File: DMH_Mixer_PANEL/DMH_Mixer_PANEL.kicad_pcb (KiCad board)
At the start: 2 copper layers, 50 x 200 mm, 5 parts, among them J0 Panel_GND_Solder_Wire_Pad

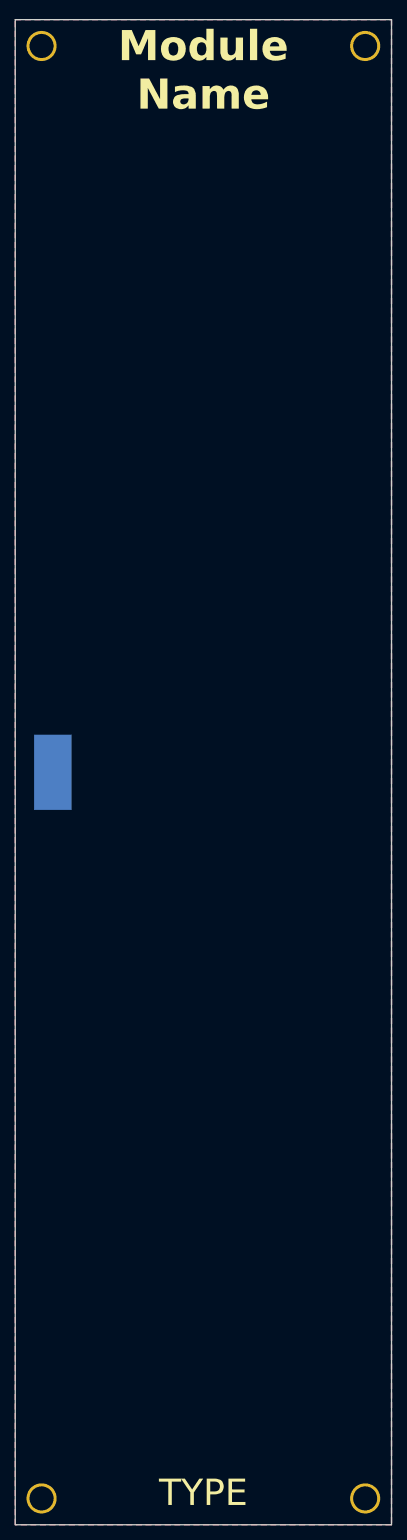
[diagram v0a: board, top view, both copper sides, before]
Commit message: Designed mixer front panel
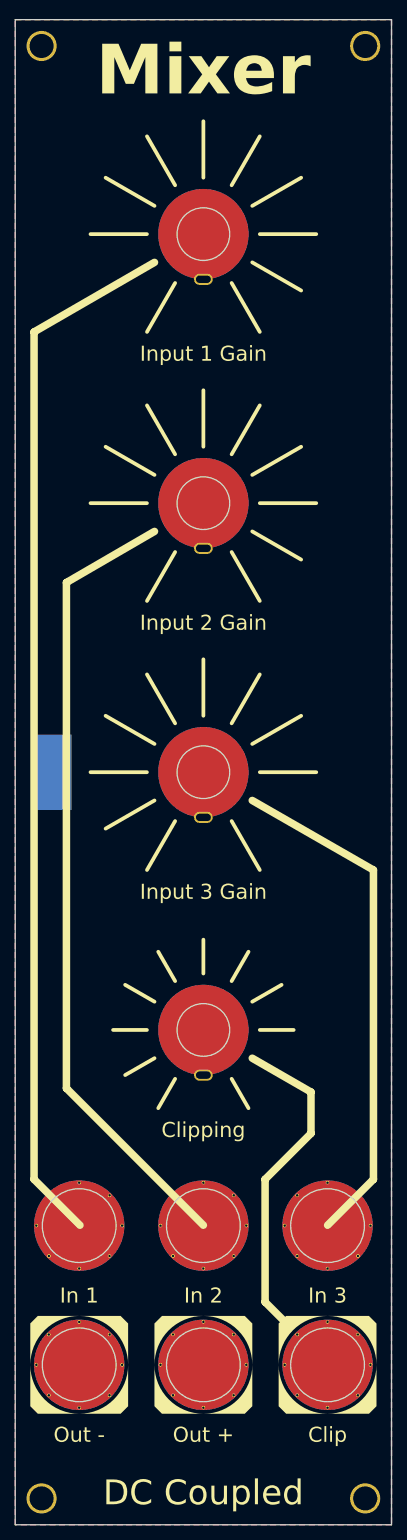
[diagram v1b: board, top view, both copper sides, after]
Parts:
- added H10: Clip, SynthStuff:Jack_6.35mm_Cutout_Output_v6, F.Cu at (91.5, 208.8)
- added H11: Input 1 Gain, SynthStuff:Pot_Cutout_Small, F.Cu at (75.0, 58.5)
- added H12: Input 2 Gain, SynthStuff:Pot_Cutout_Small, F.Cu at (75.0, 94.2)
- added H13: Input 3 Gain, SynthStuff:Pot_Cutout_Small, F.Cu at (75.0, 130.0)
- added H14: Clipping, SynthStuff:Pot_Cutout_Tiny, F.Cu at (75.0, 164.2)
- added H5: In 1, SynthStuff:Jack_6.35mm_Cutout_v3, F.Cu at (58.5, 190.2)
- added H6: In 2, SynthStuff:Jack_6.35mm_Cutout_v3, F.Cu at (75.0, 190.2)
- added H7: In 3, SynthStuff:Jack_6.35mm_Cutout_v3, F.Cu at (91.5, 190.2)
- added H8: Out +, SynthStuff:Jack_6.35mm_Cutout_Output_v6, F.Cu at (75.0, 208.8)
- added H9: Out -, SynthStuff:Jack_6.35mm_Cutout_Output_v6, F.Cu at (58.5, 208.8)
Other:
- board text added: "DC Coupled"
- board text added: "Mixer"
- board text removed: "Module Name"
- board text removed: "TYPE"

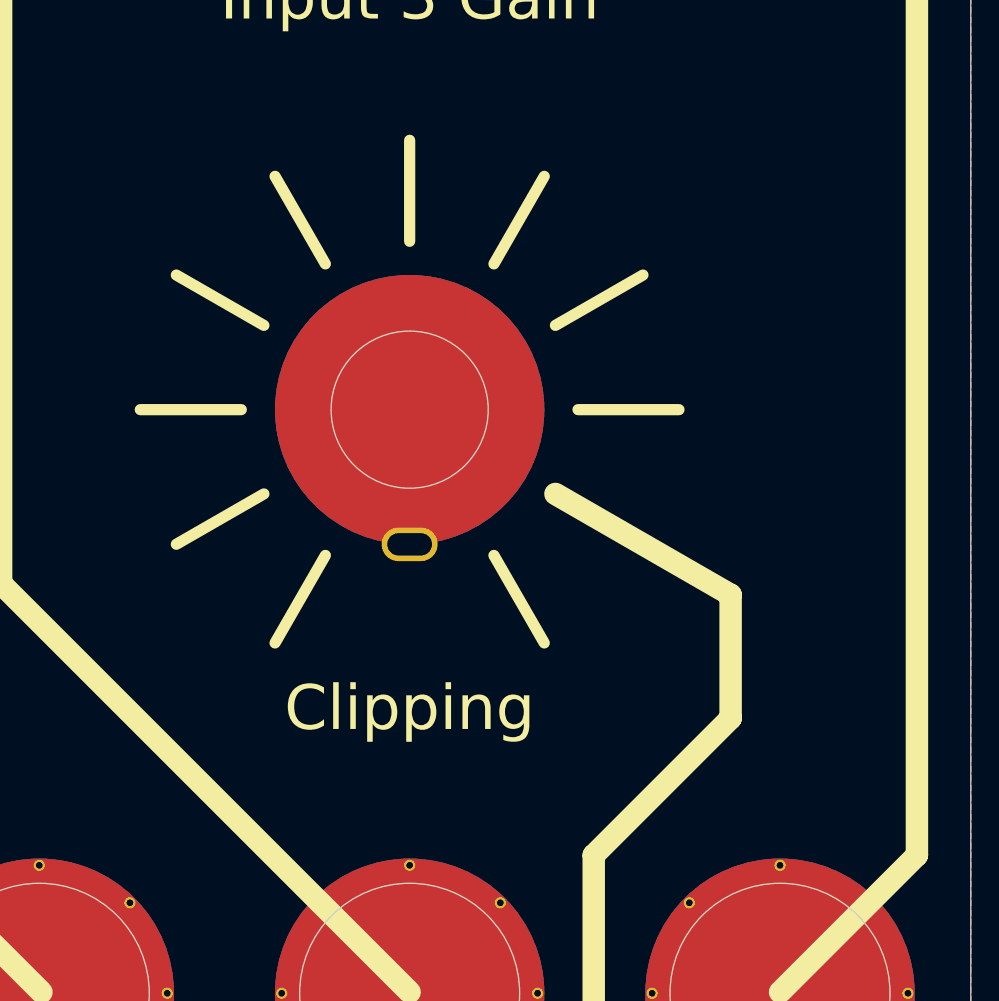
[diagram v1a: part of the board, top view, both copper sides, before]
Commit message: Moved clipping knob to the right
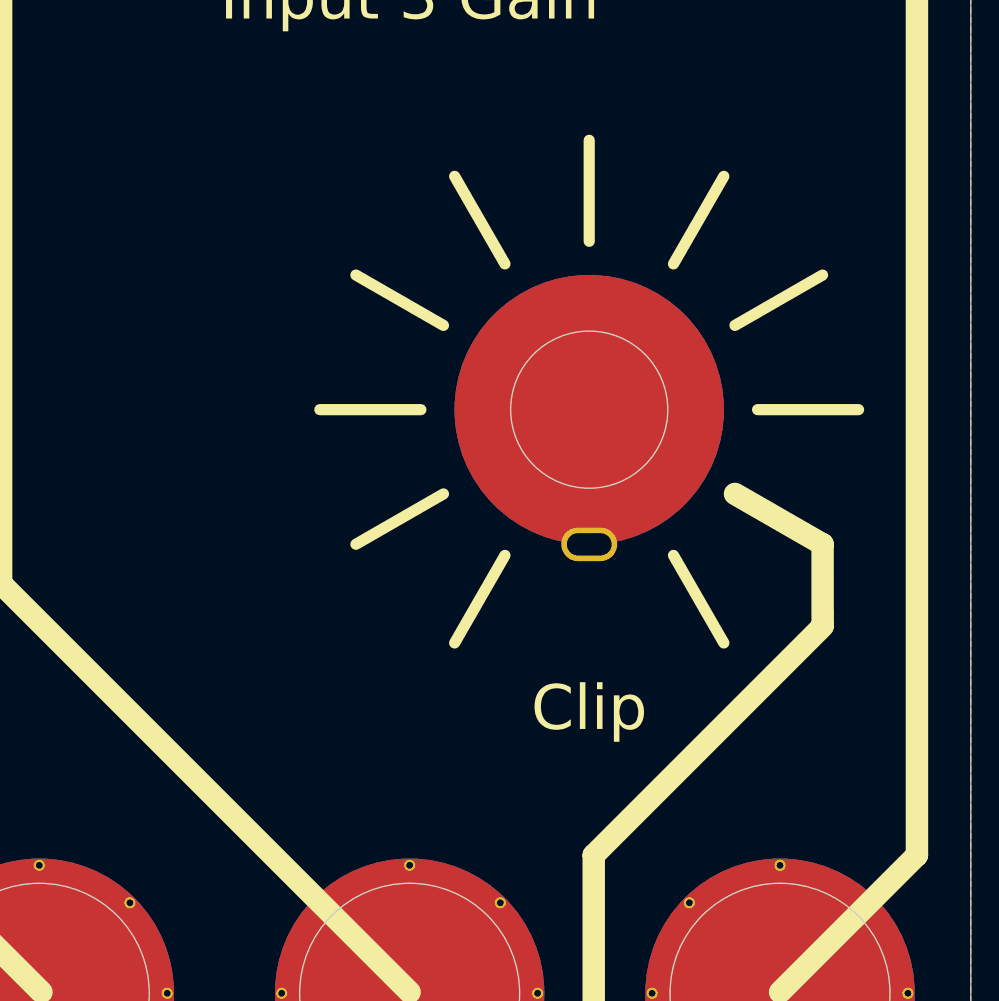
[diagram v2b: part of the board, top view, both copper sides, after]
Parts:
- H14: value Clipping -> Clip
- moved H14 8.00 mm to (83.0, 164.2)
